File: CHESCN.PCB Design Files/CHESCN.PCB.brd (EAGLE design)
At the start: 35 x 80 mm, 78 parts

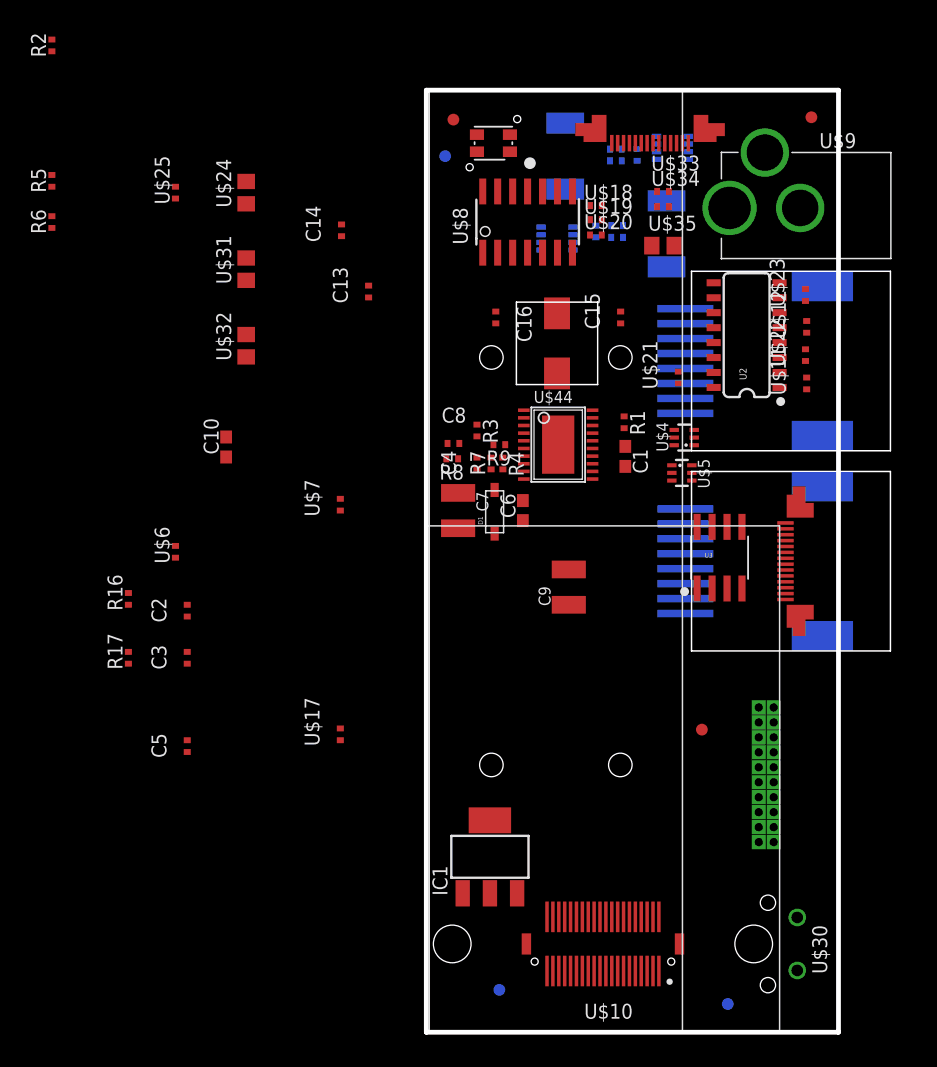
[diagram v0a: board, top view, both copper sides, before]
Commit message: Routing complete
Finished rounting. Requires 0.15mm milling and 0.25mm vias
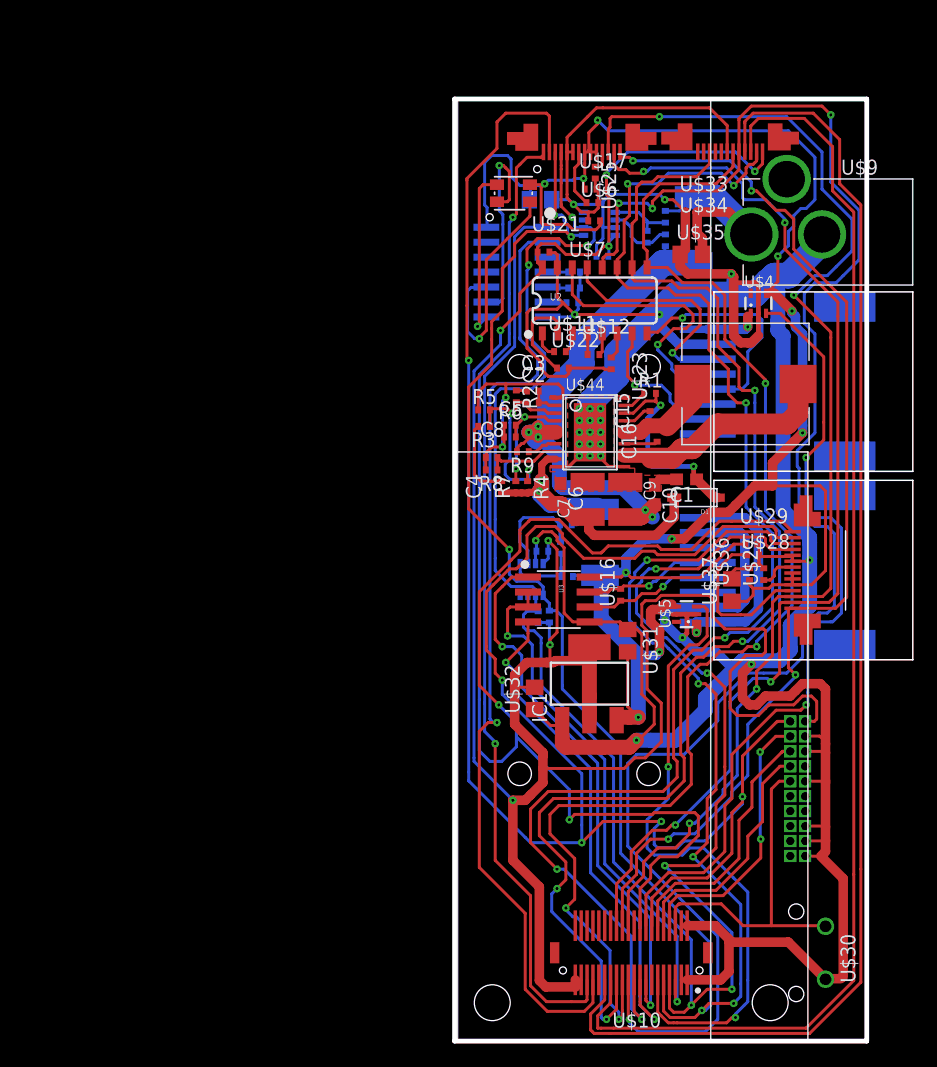
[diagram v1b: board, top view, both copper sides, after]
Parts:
- removed U$38, U$39, U$40, U$41, U$42, U$43: (no value), adafruit:FIDUCIAL_1MM
- added U$16: 120, GW-devices:RF-R0402
- added U$26: SFV12R-1STE1HLF, KW2:SFV12R-1STE1HLF
- added U$27, U$28: 10k, GW-devices:RF-R0402
- added U$29: 0.1uF, GW-devices:C0402
- added U$36: 1uF, GW-devices:C0402
- added U$37: 10uF, GW-devices:C0805
- C1, C10, C6: value (none) -> 1uF
- C11, C12, C13, C14, C15, C16: value (none) -> 0.1uF
- C2: value (none) -> 10pF
- C3: value (none) -> 680pF
- C4: value (none) -> 47pF
- C5, C8: value (none) -> 100pF
- C7, C9: value (none) -> 47uF
- R1, R7, R9: value (none) -> 1M
- R12, R13, R14, R15: value (none) -> 10
- R16, R17: value (none) -> 3.3k
- R2: value (none) -> 33k
- R3: value (none) -> 10k
- R4: value (none) -> 845k
- R5: value (none) -> 158k
- R6: value (none) -> 133k
- R8: value (none) -> 42.2k
- U$10: value (none) -> DF12_FOLD; device KW2:DF12_F -> KW2:BRAIN_OLD
- U$15: value 744311470 -> 744311470S; device KW2:744311470 -> KW2:IHLP4040DZ
- moved U$17 50.9 mm to (74.0, 81.6), turned to 0 degrees
- moved R2 49.4 mm to (67.7, 64.0), turned to 270 degrees
- moved U$6 46.2 mm to (74.1, 80.5), turned to 0 degrees
- moved U$31 45.2 mm to (77.1, 43.2), turned to 270 degrees
- moved R6 42.6 mm to (67.1, 61.5), turned to 0 degrees
- moved R5 41.5 mm to (64.9, 62.9), turned to 0 degrees
- moved U$32 38.7 mm to (69.2, 38.4)
- moved U$46 38.5 mm to (69.0, 48.5), turned to 180 degrees
- moved C5 37.9 mm to (67.1, 60.5), turned to 0 degrees
- moved C3 37.1 mm to (69.0, 64.5), turned to 0 degrees
- moved C10 36.6 mm to (79.4, 55.6), turned to 270 degrees
- moved R17 35.9 mm to (70.5, 45.3), flipped to the bottom, turned to 270 degrees
- moved U$25 35.7 mm to (74.3, 83.0), turned to 270 degrees
- moved R14 35.5 mm to (72.0, 48.7), turned to 180 degrees
- moved R16 34.8 mm to (69.5, 45.2), flipped to the bottom, turned to 270 degrees
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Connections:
- new net N$52: SCANNER.P$5, U2.8
- new net N$54: U$10.P$23, U$26.P$6, U2.9
- new net N$62: U$10.P$29, U$26.P$4
- new net N$63: U$14.P$4, U$28.1
- new net N$64: U$14.P$8, U$27.1
- net +3V3: now also U$26.P$1
- net +5V: now also U$29.1, U$36.1, U$37.1
- net GND: now also U$26.P$7, U$27.2, U$28.2, U$29.2, U$36.2, U$37.2; no longer U2.8
- net N$1: now also U$14.P$13, U$2.P$13
- net N$10: now also U$26.P$5
- net N$19: now also U$16.2
- net N$20: now also U$16.1
- net N$26: now also U$26.P$2
- net N$33: no longer U$14.P$4
- net N$34: no longer U$14.P$8
- net N$41: now also U$26.P$10
- net N$60: now also U$10.P$27, U$26.P$3; no longer U$14.P$13, U$2.P$13
- net N$61: now also U$10.P$18
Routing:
- net GND: track 0.00 -> 379.8 mm, vias 0 -> 28
- net +3V3: track 0.00 -> 203.4 mm, vias 0 -> 7
- net N$1: track 0.00 -> 178.3 mm, vias 0 -> 5
- net +5V: track 0.00 -> 177.1 mm, vias 0 -> 10
- net N$58: track 0.00 -> 162.8 mm, vias 0 -> 8
- net N$59: track 0.00 -> 160.2 mm, vias 0 -> 8
- net N$10: track 0.00 -> 142.2 mm, vias 0 -> 4
- net N$61: track 0.00 -> 137.9 mm, vias 0 -> 3
- net N$26: track 0.00 -> 118.5 mm, vias 0 -> 6
- net N$62: track 0.00 -> 113.8 mm
- net N$41: track 0.00 -> 111.2 mm, vias 0 -> 4
- net N$54: track 0.00 -> 110.3 mm, vias 0 -> 4
- net N$60: track 0.00 -> 109.9 mm
- net N$31: track 0.00 -> 103.5 mm, vias 0 -> 4
- net N$29: track 0.00 -> 92.8 mm, vias 0 -> 4
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- added copper zone on layer 1, net GND

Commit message: Pre-fab, added headers
Need to export production files
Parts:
- added JP1, JP2: (no value), SparkFun:1X02_PP_HOLES_ONLY
- added U$38: 10k, GW-devices:RF-R0402
- moved U$30 0.75 mm to (93.9, 17.5)
- moved U$17 0.58 mm to (74.2, 81.1)
- moved U$6 0.45 mm to (74.3, 80.0)
- moved U$7 0.10 mm to (74.2, 78.8)
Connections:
- net +3V3: now also U$38.2
- net GND: now also JP1.2, JP2.2
- net N$60: now also JP2.1, U$38.1
- net V+: now also JP1.1
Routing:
- net GND: track 379.8 -> 444.5 mm
- net V+: track 18.3 -> 39.0 mm
- net N$60: track 109.9 -> 117.7 mm, vias 0 -> 1
- net N$31: track 103.5 -> 109.4 mm
- net +3V3: track 203.4 -> 208.9 mm, vias 7 -> 8
- net N$6: track 28.7 -> 26.8 mm
- net N$41: track 111.2 -> 110.1 mm
- net +5V: track 177.1 -> 176.1 mm
- net N$10: track 142.2 -> 141.2 mm
- net N$26: track 118.5 -> 117.8 mm
- net N$1: track 178.3 -> 177.6 mm
- net N$34: track 4.86 -> 5.37 mm
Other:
- board text added: "CHESCN.PCB.v1.0"
- board text added: "R.S. 6/19/2015"

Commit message: Various fixes + BL board
Fixed consistency issues (diode, inductor), added laser test files and
added backlight board
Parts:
- added U$39: 744311470S, KW2:IHLP4040DZ
- U$15: value 744311470S -> SOD128; device KW2:IHLP4040DZ -> KW2:SOD128
- moved U$15 27.2 mm to (69.6, 85.9), flipped to the bottom
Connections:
- new net N$65: JP1.1, U$15.P$2
- net N$32: now also U$39.P$1; no longer U$15.P$1
- net N$35: now also U$39.P$2; no longer U$15.P$2
- net V+: now also U$15.P$1; no longer JP1.1
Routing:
- net V+: track 39.0 -> 31.7 mm
- net N$65: track 0.00 -> 3.43 mm
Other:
- board text added: "+"
- board text added: "-"
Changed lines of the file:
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@@
 <?xml version="1.0" encoding="utf-8"?>
 <!DOCTYPE eagle SYSTEM "eagle.dtd">
-<eagle version="6.5.0">
+<eagle version="6.6.0">
 <drawing>
 <settings>
@@
 <layer number="23" name="tOrigins" color="15" fill="1" visible="yes" active="yes"/>
 <layer number="24" name="bOrigins" color="15" fill="1" visible="yes" active="yes"/>
-<layer number="25" name="tNames" color="7" fill="1" visible="no" active="yes"/>
-<layer number="26" name="bNames" color="7" fill="1" visible="no" active="yes"/>
-<layer number="27" name="tValues" color="7" fill="1" visible="no" active="yes"/>
-<layer number="28" name="bValues" color="7" fill="1" visible="no" active="yes"/>
-<layer number="29" name="tStop" color="7" fill="3" visible="no" active="yes"/>
-<layer number="30" name="bStop" color="7" fill="6" visible="no" active="yes"/>
-<layer number="31" name="tCream" color="7" fill="4" visible="no" active="yes"/>
-<layer number="32" name="bCream" color="7" fill="5" visible="no" active="yes"/>
-<layer number="33" name="tFinish" color="6" fill="3" visible="no" active="yes"/>
-<layer number="34" name="bFinish" color="6" fill="6" visible="no" active="yes"/>
+<layer number="25" name="tNames" color="7" fill="1" visible="yes" active="yes"/>
+<layer number="26" name="bNames" color="7" fill="1" visible="yes" active="yes"/>
+<layer number="27" name="tValues" color="7" fill="1" visible="yes" active="yes"/>
+<layer number="28" name="bValues" color="7" fill="1" visible="yes" active="yes"/>
+<layer number="29" name="tStop" color="7" fill="3" visible="yes" active="yes"/>
+<layer number="30" name="bStop" color="7" fill="6" visible="yes" active="yes"/>
+<layer number="31" name="tCream" color="7" fill="4" visible="yes" active="yes"/>
+<layer number="32" name="bCream" color="7" fill="5" visible="yes" active="yes"/>
+<layer number="33" name="tFinish" color="6" fill="3" visible="yes" active="yes"/>
+<layer number="34" name="bFinish" color="6" fill="6" visible="yes" active="yes"/>
 <layer number="35" name="tGlue" color="7" fill="4" visible="yes" active="yes"/>
 <layer number="36" name="bGlue" color="7" fill="5" visible="yes" active="yes"/>
@@
 <wire x1="97.4" y1="9.25" x2="62.4" y2="9.25" width="0.4064" layer="20"/>
 <wire x1="62.4" y1="9.25" x2="62.4" y2="89.25" width="0.4064" layer="20"/>
-<wire x1="63" y1="120" x2="96" y2="120" width="0.4064" layer="206"/>
-<wire x1="63" y1="120" x2="63" y2="95" width="0.4064" layer="206"/>
-<wire x1="96" y1="120" x2="96" y2="95" width="0.4064" layer="206"/>
-<wire x1="96" y1="95" x2="63" y2="95" width="0.4064" layer="206"/>
 <hole x="89.2" y="16.75" drill="3.048"/>
 <hole x="65.6" y="16.75" drill="3.048"/>
@@
 <text x="94.9" y="23.3" size="1.27" layer="21" font="vector" rot="R90">CHESCN.PCB.v1.0</text>
 <text x="96.3" y="26.6" size="0.8128" layer="21" font="vector" rot="R90">R.S. 6/19/2015</text>
+<rectangle x1="72.5" y1="58.5" x2="75.3" y2="63.4" layer="16"/>
+<text x="63.7" y="82.2" size="1.778" layer="21" font="vector">+</text>
+<text x="65.4" y="86.7" size="1.778" layer="21" font="vector">-</text>
 </plain>
 <attributes>
@@
 <param name="mlMinCreamFrame" value="0mil"/>
 <param name="mlMaxCreamFrame" value="0mil"/>
-<param name="mlViaStopLimit" value="0mil"/>
+<param name="mlViaStopLimit" value="0.26mm"/>
 <param name="srRoundness" value="0"/>
 <param name="srMinRoundness" value="0mil"/>
@@
 <element name="C13" library="GW-devices" package="C0402" value="0.1uF" x="74.95" y="75.9" rot="MR0"/>
 <element name="C14" library="GW-devices" package="C0402" value="0.1uF" x="69.85" y="50.85" rot="MR0"/>
-<element name="U$15" library="KW2" package="IHLP4040DZ" value="744311470S" x="87.1" y="65.05"/>
 <element name="C15" library="GW-devices" package="C0402" value="0.1uF" x="79" y="62.25" rot="R90"/>
 <element name="C16" library="GW-devices" package="C0402" value="0.1uF" x="79.6" y="59.65" rot="R90"/>
@@
 <element name="JP2" library="SparkFun" package="1X02_PP_HOLES_ONLY" value="" x="69.1" y="10.9"/>
 <element name="JP1" library="SparkFun" package="1X02_PP_HOLES_ONLY" value="" x="64.3" y="85.1" rot="R90"/>
+<element name="U$15" library="KW2" package="SOD128" value="SOD128" x="69.6" y="85.9" rot="MR0"/>
+<element name="U$39" library="KW2" package="IHLP4040DZ" value="744311470S" x="87.1" y="65.1"/>
 </elements>
 <signals>
@@
 <wire x1="83.4" y1="77.45" x2="83.45" y2="77.4" width="0.8128" layer="1"/>
 <wire x1="83.45" y1="77.4" x2="83.45" y2="76.05" width="0.8128" layer="1"/>
-<contactref element="JP1" pad="1"/>
 <wire x1="82.7" y1="80.95" x2="81.55" y2="82.1" width="1.016" layer="16"/>
 <wire x1="81.55" y1="82.1" x2="78.9" y2="82.1" width="1.016" layer="16"/>
 <wire x1="78.9" y1="82.1" x2="74.9" y2="82.1" width="1.016" layer="16"/>
-<wire x1="74.9" y1="82.1" x2="71.2" y2="85.8" width="1.016" layer="16"/>
-<wire x1="71.2" y1="85.8" x2="66.4" y2="85.8" width="1.016" layer="16"/>
-<wire x1="66.4" y1="85.8" x2="65" y2="85.8" width="1.016" layer="16"/>
-<wire x1="65" y1="85.8" x2="64.3" y2="85.1" width="1.016" layer="16"/>
+<contactref element="U$15" pad="P$1"/>
+<wire x1="74.9" y1="82.1" x2="71.8" y2="85.2" width="1.016" layer="16"/>
+<wire x1="71.8" y1="85.2" x2="71.8" y2="85.9" width="1.016" layer="16"/>
 </signal>
 <signal name="N$13">
@@
 <contactref element="U$44" pad="16"/>
 <contactref element="U$44" pad="15"/>
-<contactref element="U$15" pad="P$1"/>
 <contactref element="C15" pad="1"/>
 <wire x1="76.8" y1="60.95" x2="77.6" y2="60.95" width="1.27" layer="1"/>
@@
 <wire x1="79" y1="61.75" x2="79" y2="61.6" width="0.254" layer="1"/>
 <wire x1="79" y1="61.6" x2="78.9" y2="61.5" width="0.254" layer="1"/>
+<contactref element="U$39" pad="P$1"/>
+<wire x1="82.6295" y1="65.05" x2="82.6295" y2="65.1" width="0" layer="19" extent="1-1"/>
 </signal>
 <signal name="N$35">
 <contactref element="U$44" pad="13"/>
 <contactref element="U$44" pad="12"/>
-<contactref element="U$15" pad="P$2"/>
 <contactref element="C16" pad="1"/>
 <wire x1="80.9" y1="58.75" x2="79.1" y2="58.75" width="1.778" layer="1"/>
@@
 <wire x1="91.5705" y1="65.05" x2="91.5705" y2="62.5705" width="1.778" layer="1"/>
 <wire x1="91.5705" y1="62.5705" x2="90.65" y2="61.65" width="1.778" layer="1"/>
+<contactref element="U$39" pad="P$2"/>
+<wire x1="91.5705" y1="65.05" x2="91.5705" y2="65.1" width="0" layer="19" extent="1-1"/>
 </signal>
 <signal name="N$36">
@@
 <wire x1="89.2" y1="48.4" x2="88.65" y2="48.4" width="0.254" layer="1"/>
 </signal>
+<signal name="N$65">
+<contactref element="JP1" pad="1"/>
+<wire x1="64.3" y1="85.1" x2="64.9" y2="85.7" width="1.016" layer="16"/>
+<contactref element="U$15" pad="P$2"/>
+<wire x1="64.9" y1="85.7" x2="65.1" y2="85.9" width="1.016" layer="16"/>
+<wire x1="65.1" y1="85.9" x2="67.4" y2="85.9" width="1.016" layer="16"/>
+</signal>
 </signals>
